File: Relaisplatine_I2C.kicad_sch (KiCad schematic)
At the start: 31 parts, among them J1 J, J1.1 G1-J, J1.2 G1-K, J1001 Conn_01x08, J2 K, J2.1 G2-J, J2.2 G2-K, J3.1 G3-J, J3.2 G3-K, J4.1 G4-J, J4.2 G4-K, J5.1 G5-J, J5.2 G5-K, J6.1 G6-J, J6.2 G6-K, J7.1 G7-J, J7.2 G7-K, J8.1 G8-J, J8.2 G8-K, U1 ULN2803A, U2 PCF8574

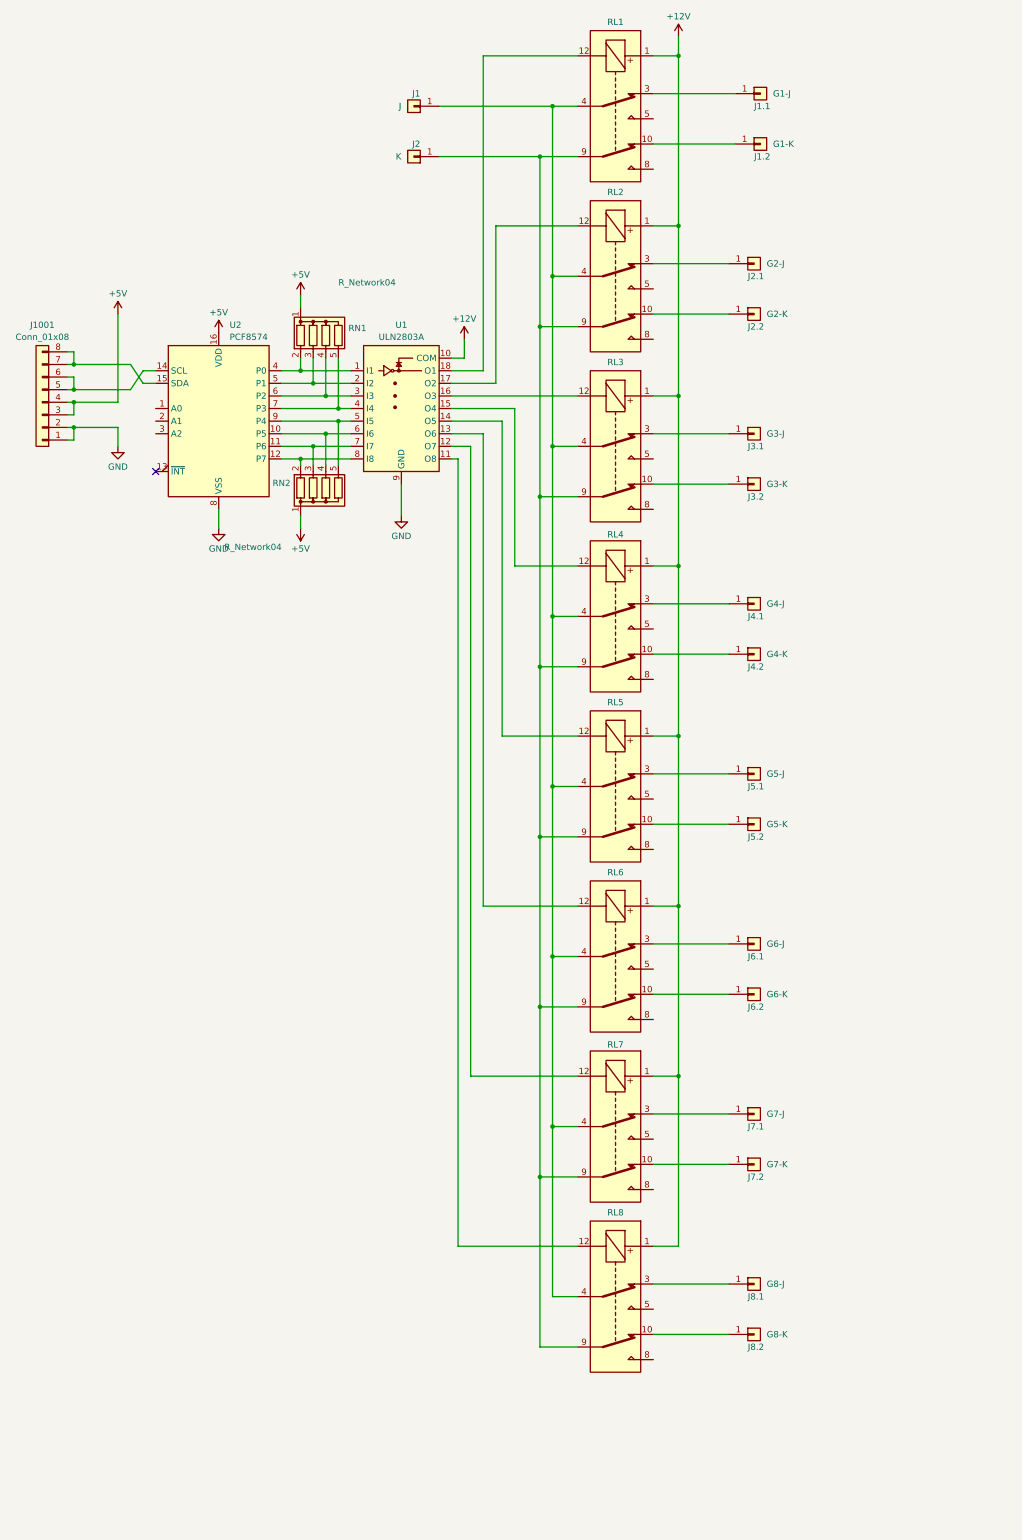
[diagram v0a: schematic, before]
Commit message: Pins für A0-2 beschltet
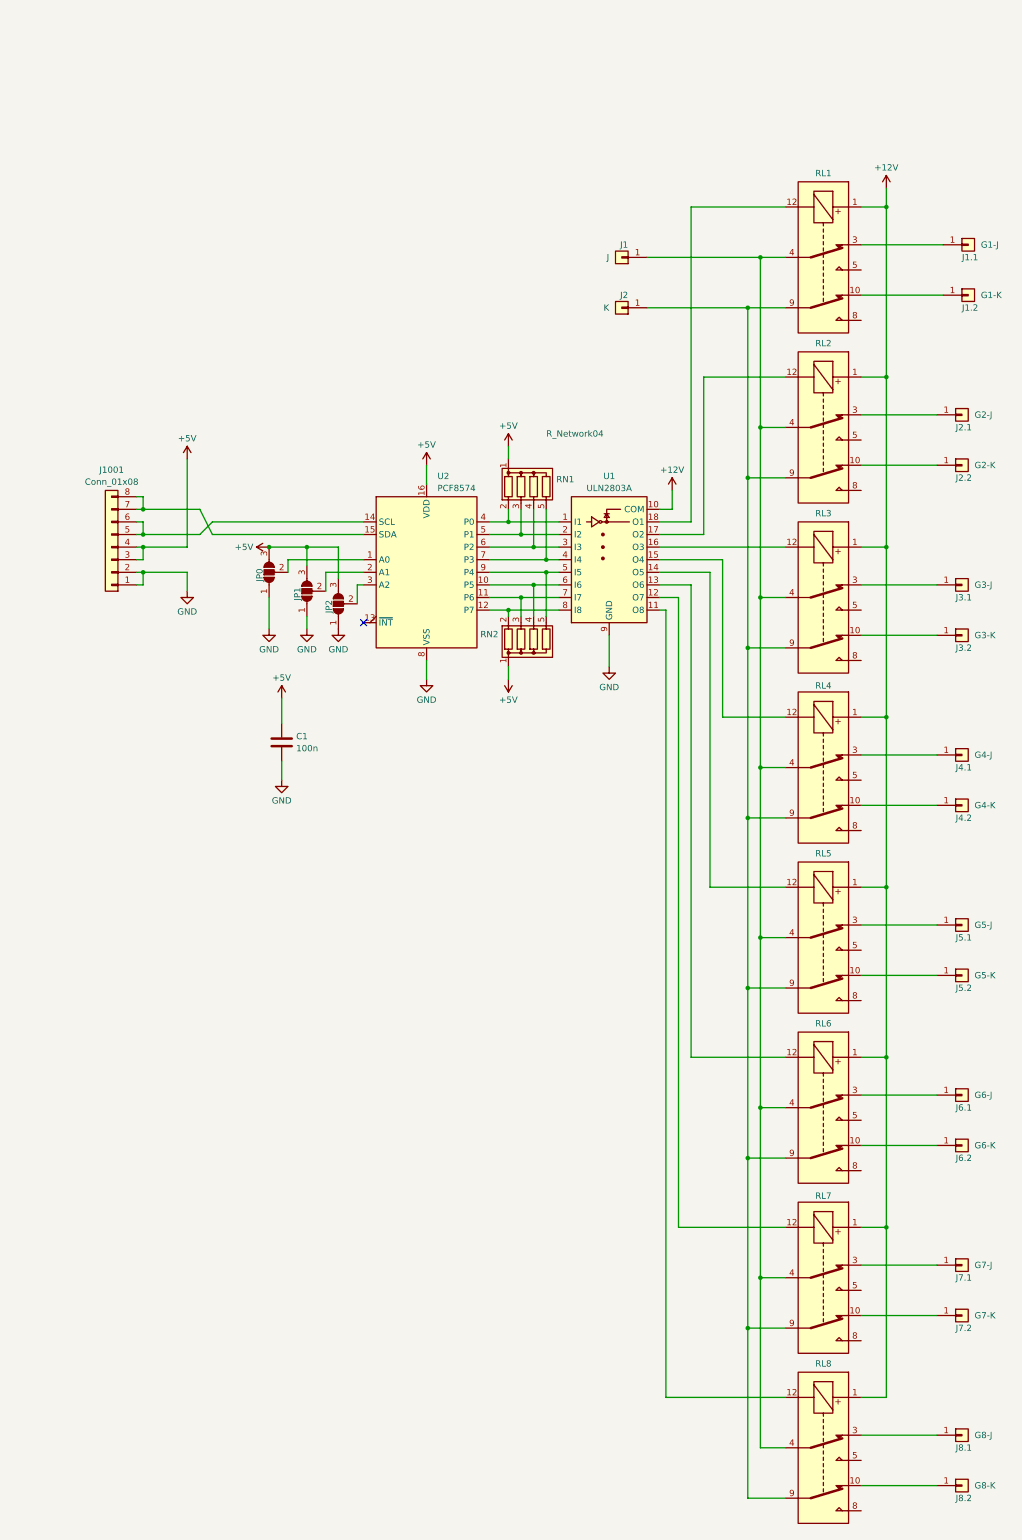
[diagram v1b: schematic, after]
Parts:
- added C1: 100n, Capacitor_THT:C_Disc_D6.0mm_W2.5mm_P5.00mm, symbol Device:C
- added JP0, JP1, JP2: SolderJumper_3_Open, Jumper:SolderJumper-3_P1.3mm_Bridged12_Pad1.0x1.5mm_NumberLabels, symbol Jumper:SolderJumper_3_Open
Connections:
- net +5V: now also C1.1, JP0.3 (B), JP1.3 (B), JP2.3 (B)
- net GND: now also C1.2, JP0.1 (A), JP1.1 (A), JP2.1 (A)
- net at U2.1 (A0): now also JP0.2 (C)
- net at U2.2 (A1): now also JP1.2 (C)
- net at U2.3 (A2): now also JP2.2 (C)
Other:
- moved on the sheet: J1, J1.1, J1.2, J1001, J2, J2.1, J2.2, J3.1, J3.2, J4.1, J4.2, J5.1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

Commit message: Unbekannte Änderungen
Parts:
- added D1, D2, D3, D4, D5, D6, D7, D8: LED, LED_SMD:LED_0805_2012Metric_Pad1.15x1.40mm_HandSolder, symbol Device:LED
- added H1, H2, H3, H4: MountingHole, MountingHole:MountingHole_3.2mm_M3, symbol Mechanical:MountingHole
- added J1.1a1001, J1.2a1002, J1.2a1003, J1.2a1004, J1.2a1005, J1.2a1006, J1.2a1007, J2.1a1001: G1-J, Connector_Pin:Pin_D1.1mm_L8.5mm_W2.5mm_FlatFork, symbol Connector_Generic:Conn_01x01
- added J1.1a1002, J1.1a1003, J1.1a1004, J1.1a1005, J1.1a1006, J1.1a1007, J1.2a1001: G1-K, Connector_Pin:Pin_D1.1mm_L8.5mm_W2.5mm_FlatFork, symbol Connector_Generic:Conn_01x01
- added J11: Relais-Power, Connector_PinHeader_2.54mm:PinHeader_2x02_P2.54mm_Horizontal, symbol Connector_Generic:Conn_01x04
- added J2.2a1001: G2-K, Connector_Pin:Pin_D1.1mm_L8.5mm_W2.5mm_FlatFork, symbol Connector_Generic:Conn_01x01
- added R1, R2, R3, R4, R5, R6, R7, R8: 1k, Resistor_SMD:R_0805_2012Metric_Pad1.20x1.40mm_HandSolder, symbol Device:R
- J1: value J -> K
- J1.1: value G1-J -> G1-K
- J1.2: value G1-K -> G1-J
- J10: renamed from J1001; value Conn_01x08 -> I²C
- J2: value K -> J
- J2.1: value G2-J -> G2-K
- J2.2: value G2-K -> G2-J
- J3.1: value G3-J -> G3-K
- J3.2: value G3-K -> G3-J
- J4.1: value G4-J -> G4-K
- J4.2: value G4-K -> G4-J
- J5.1: value G5-J -> G5-K
- J5.2: value G5-K -> G5-J
- J6.1: value G6-J -> G6-K
- J6.2: value G6-K -> G6-J
- J7.1: value G7-J -> G7-K
- J7.2: value G7-K -> G7-J
- J8.1: value G8-J -> G8-K
- J8.2: value G8-K -> G8-J
- renumbered JP0 to A0, JP1 to A1, JP2 to A2
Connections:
- net +12V: now also J11.3 (Pin_3), J11.4 (Pin_4), R1.1, R2.1, R3.1, R4.1, R5.1, R6.1, R7.1, R8.1
- net GND: now also J11.1 (Pin_1), J11.2 (Pin_2)
- net at RL6.12, U1.13 (O6): now also D6.1 (K)
- net at RL6.5: now also J1.1a1005.1 (Pin_1)
- net at RL6.8: now also J1.2a1005.1 (Pin_1)
- net at RL4.12, U1.15 (O4): now also D4.1 (K)
- net at RL4.5: now also J1.1a1003.1 (Pin_1)
- net at RL4.8: now also J1.2a1003.1 (Pin_1)
- net at RL8.12, U1.11 (O8): now also D8.1 (K)
- net at RL8.5: now also J1.1a1007.1 (Pin_1)
- net at RL8.8: now also J1.2a1007.1 (Pin_1)
- net at RL5.12, U1.14 (O5): now also D5.1 (K)
- net at RL5.5: now also J1.1a1004.1 (Pin_1)
- net at RL5.8: now also J1.2a1004.1 (Pin_1)
- net at RL1.12, U1.18 (O1): now also D1.1 (K)
- net at RL1.5: now also J1.2a1001.1 (Pin_1)
- net at RL1.8: now also J1.1a1001.1 (Pin_1)
- net at RL7.12, U1.12 (O7): now also D7.1 (K)
- net at RL3.12, U1.16 (O3): now also D3.1 (K)
- net at RL2.12, U1.17 (O2): now also D2.1 (K)
- net at RL2.5: now also J2.2a1001.1 (Pin_1)
- net at RL2.8: now also J2.1a1001.1 (Pin_1)
- net at RL3.5: now also J1.1a1002.1 (Pin_1)
- net at RL3.8: now also J1.2a1002.1 (Pin_1)
- net at RL7.5: now also J1.1a1006.1 (Pin_1)
- net at RL7.8: now also J1.2a1006.1 (Pin_1)
- new net: D4.2 (A), R4.2
- new net: D7.2 (A), R7.2
- new net: D3.2 (A), R3.2
- new net: D1.2 (A), R1.2
- new net: D8.2 (A), R8.2
- new net: D5.2 (A), R5.2
- new net: D6.2 (A), R6.2
- new net: D2.2 (A), R2.2
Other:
- moved on the sheet: RL1, RL2, RL3, RL4, RL5, RL6, RL7, RL8

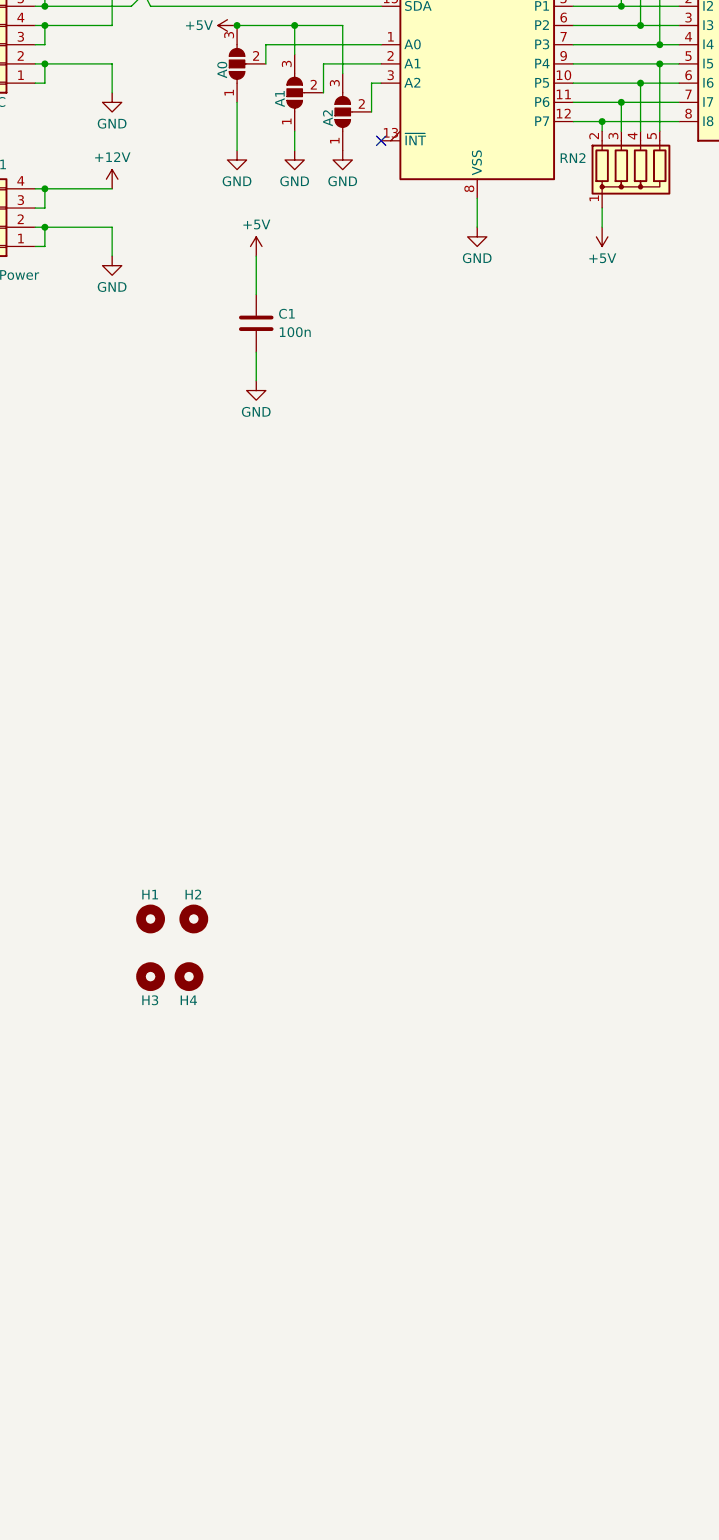
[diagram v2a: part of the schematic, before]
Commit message: Int-Pin herausgezogen und Kosmetik
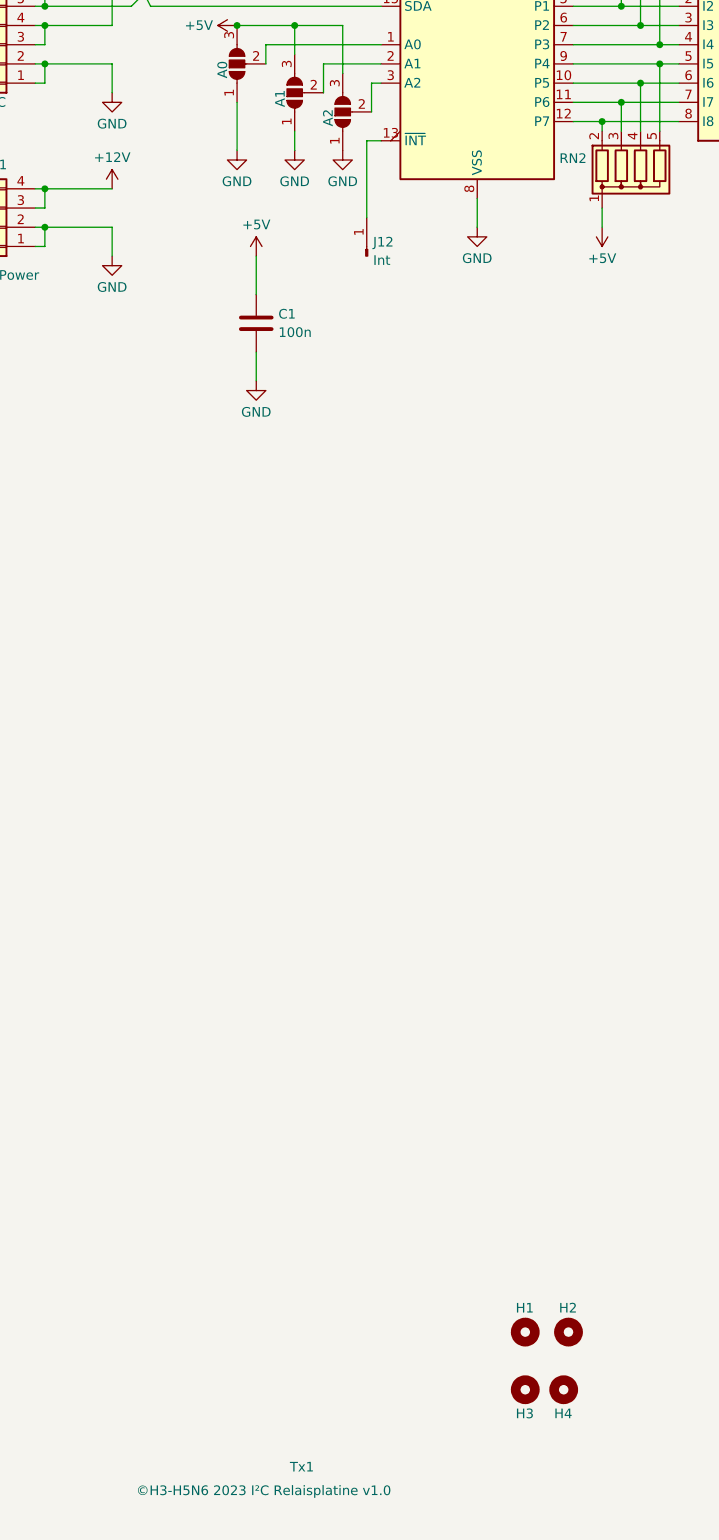
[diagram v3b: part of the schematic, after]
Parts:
- added J12: Int, Connector_PinHeader_2.54mm:PinHeader_1x01_P2.54mm_Vertical, symbol Connector:Conn_01x01_Pin
- added Tx1: ©H3-H5N6 2023 I²C Relaisplatine v1.0, Text:Text, symbol Text:Text
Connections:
- net at U2.13 (~{INT}): now also J12.1 (Pin_1)
- no-connect marks 1 -> 0
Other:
- title: (none) -> I²C 8-fach Railsplatine
- moved on the sheet: H1, H2, H3, H4
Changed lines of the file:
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@@
 (kicad_sch (version 20230121) (generator eeschema)
   (paper "A3" portrait)
+  (title_block
+    (title "I²C 8-fach Railsplatine")
+    (date "2023-12-03")
+  )
   (junction (at 187.96 193.04) (diameter 0) (color 0 0 0 0)
   )
@@
   (junction (at 165.735 179.07) (diameter 0) (color 0 0 0 0)
   )
-  (no_connect (at 82.55 139.7))
   (wire (pts (xy 143.51 316.865) (xy 143.51 316.23))
     (stroke (width 0) (type default))
@@
     (stroke (width 0) (type default))
   )
+  (wire (pts (xy 80.645 139.7) (xy 80.645 149.86))
+    (stroke (width 0) (type default))
+  )
   (wire (pts (xy 158.115 37.465) (xy 162.56 37.465))
     (stroke (width 0) (type default))
@@
     (stroke (width 0) (type default))
   )
+  (wire (pts (xy 82.55 139.7) (xy 80.645 139.7))
+    (stroke (width 0) (type default))
+  )
   (wire (pts (xy 148.59 37.465) (xy 153.67 37.465))
     (stroke (width 0) (type default))
@@
     )
   )
-  (symbol (lib_id "Mechanical:MountingHole") (at 57.785 242.57 0) (unit 1)
+  (symbol (lib_id "Mechanical:MountingHole") (at 107.315 297.18 0) (unit 1)
     (in_bom yes) (on_board yes) (dnp no)
-    (property "Reference" "H2" (at 56.515 239.395 0)
+    (property "Reference" "H2" (at 106.045 294.005 0)
       (effects (font (size 1.27 1.27)) (justify left))
     )
-    (property "Value" "MountingHole" (at 60.325 243.7821 0)
+    (property "Value" "MountingHole" (at 109.855 298.3921 0)
       (effects (font (size 1.27 1.27)) (justify left) hide)
     )
-    (property "Footprint" "MountingHole:MountingHole_3.2mm_M3" (at 57.785 242.57 0)
+    (property "Footprint" "MountingHole:MountingHole_3.2mm_M3" (at 107.315 297.18 0)
       (effects (font (size 1.27 1.27)) hide)
     )
-    (property "Datasheet" "~" (at 57.785 242.57 0)
+    (property "Datasheet" "~" (at 107.315 297.18 0)
       (effects (font (size 1.27 1.27)) hide)
     )
@@
     )
   )
-  (symbol (lib_id "Mechanical:MountingHole") (at 52.07 242.57 0) (unit 1)
+  (symbol (lib_id "Mechanical:MountingHole") (at 101.6 297.18 0) (unit 1)
     (in_bom yes) (on_board yes) (dnp no)
-    (property "Reference" "H1" (at 50.8 239.395 0)
+    (property "Reference" "H1" (at 100.33 294.005 0)
       (effects (font (size 1.27 1.27)) (justify left))
     )
-    (property "Value" "MountingHole" (at 54.61 243.7821 0)
+    (property "Value" "MountingHole" (at 104.14 298.3921 0)
       (effects (font (size 1.27 1.27)) (justify left) hide)
     )
-    (property "Footprint" "MountingHole:MountingHole_3.2mm_M3" (at 52.07 242.57 0)
+    (property "Footprint" "MountingHole:MountingHole_3.2mm_M3" (at 101.6 297.18 0)
       (effects (font (size 1.27 1.27)) hide)
     )
-    (property "Datasheet" "~" (at 52.07 242.57 0)
+    (property "Datasheet" "~" (at 101.6 297.18 0)
       (effects (font (size 1.27 1.27)) hide)
     )
@@
     )
   )
+  (symbol (lib_id "Connector:Conn_01x01_Pin") (at 80.645 154.94 90) (unit 1)
+    (in_bom yes) (on_board yes) (dnp no) (fields_autoplaced)
+    (property "Reference" "J12" (at 81.4832 153.0929 90)
+      (effects (font (size 1.27 1.27)) (justify right))
+    )
+    (property "Value" "Int" (at 81.4832 155.5171 90)
+      (effects (font (size 1.27 1.27)) (justify right))
+    )
+    (property "Footprint" "Connector_PinHeader_2.54mm:PinHeader_1x01_P2.54mm_Vertical" (at 80.645 154.94 0)
+      (effects (font (size 1.27 1.27)) hide)
+    )
+    (property "Datasheet" "~" (at 80.645 154.94 0)
+      (effects (font (size 1.27 1.27)) hide)
+    )
+    (pin "1")
+    (instances
+      (project "Relaisplatine_I2C"
+        (path "/064c37a5-963a-4246-bd9f-fec8b6e7897e"
+          (reference "J12") (unit 1)
+        )
+      )
+    )
+  )
   (symbol (lib_id "Relay:EC2-3NU") (at 179.07 134.62 270) (unit 1)
     (in_bom yes) (on_board yes) (dnp no) (fields_autoplaced)
@@
     )
   )
+  (symbol (lib_id "Text:Text") (at 69.85 316.23 0) (unit 1)
+    (in_bom yes) (on_board yes) (dnp no)
+    (property "Reference" "Tx1" (at 70.485 315.0179 0)
+      (effects (font (size 1.27 1.27)) (justify left))
+    )
+    (property "Value" "©H3-H5N6 2023 I²C Relaisplatine v1.0" (at 50.165 318.135 0)
+      (effects (font (size 1.27 1.27)) (justify left))
+    )
+    (property "Footprint" "Text:Text" (at 69.85 316.23 0)
+      (effects (font (size 1.27 1.27)) hide)
+    )
+    (property "Datasheet" "~" (at 69.85 316.23 0)
+      (effects (font (size 1.27 1.27)) hide)
+    )
+    (instances
+      (project "Relaisplatine_I2C"
+        (path "/064c37a5-963a-4246-bd9f-fec8b6e7897e"
+          (reference "Tx1") (unit 1)
+        )
+      )
+    )
+  )
   (symbol (lib_id "power:+5V") (at 46.99 106.68 0) (unit 1)
     (in_bom yes) (on_board yes) (dnp no) (fields_autoplaced)
@@
     )
   )
-  (symbol (lib_id "Mechanical:MountingHole") (at 52.07 250.19 0) (unit 1)
+  (symbol (lib_id "Mechanical:MountingHole") (at 101.6 304.8 0) (unit 1)
     (in_bom yes) (on_board yes) (dnp no)
-    (property "Reference" "H3" (at 50.8 253.365 0)
+    (property "Reference" "H3" (at 100.33 307.975 0)
       (effects (font (size 1.27 1.27)) (justify left))
     )
-    (property "Value" "MountingHole" (at 54.61 251.4021 0)
+    (property "Value" "MountingHole" (at 104.14 306.0121 0)
       (effects (font (size 1.27 1.27)) (justify left) hide)
     )
-    (property "Footprint" "MountingHole:MountingHole_3.2mm_M3" (at 52.07 250.19 0)
+    (property "Footprint" "MountingHole:MountingHole_3.2mm_M3" (at 101.6 304.8 0)
       (effects (font (size 1.27 1.27)) hide)
     )
-    (property "Datasheet" "~" (at 52.07 250.19 0)
+    (property "Datasheet" "~" (at 101.6 304.8 0)
       (effects (font (size 1.27 1.27)) hide)
     )
@@
     )
   )
-  (symbol (lib_id "Mechanical:MountingHole") (at 57.15 250.19 0) (unit 1)
+  (symbol (lib_id "Mechanical:MountingHole") (at 106.68 304.8 0) (unit 1)
     (in_bom yes) (on_board yes) (dnp no)
-    (property "Reference" "H4" (at 55.88 253.365 0)
+    (property "Reference" "H4" (at 105.41 307.975 0)
       (effects (font (size 1.27 1.27)) (justify left))
     )
-    (property "Value" "MountingHole" (at 59.69 251.4021 0)
+    (property "Value" "MountingHole" (at 109.22 306.0121 0)
       (effects (font (size 1.27 1.27)) (justify left) hide)
     )
-    (property "Footprint" "MountingHole:MountingHole_3.2mm_M3" (at 57.15 250.19 0)
+    (property "Footprint" "MountingHole:MountingHole_3.2mm_M3" (at 106.68 304.8 0)
       (effects (font (size 1.27 1.27)) hide)
     )
-    (property "Datasheet" "~" (at 57.15 250.19 0)
+    (property "Datasheet" "~" (at 106.68 304.8 0)
       (effects (font (size 1.27 1.27)) hide)
     )
